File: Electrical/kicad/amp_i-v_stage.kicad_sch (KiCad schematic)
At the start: 26 parts, among them U1 NE5534ADR, U2 NE5534ADR, U3 NE5534ADR

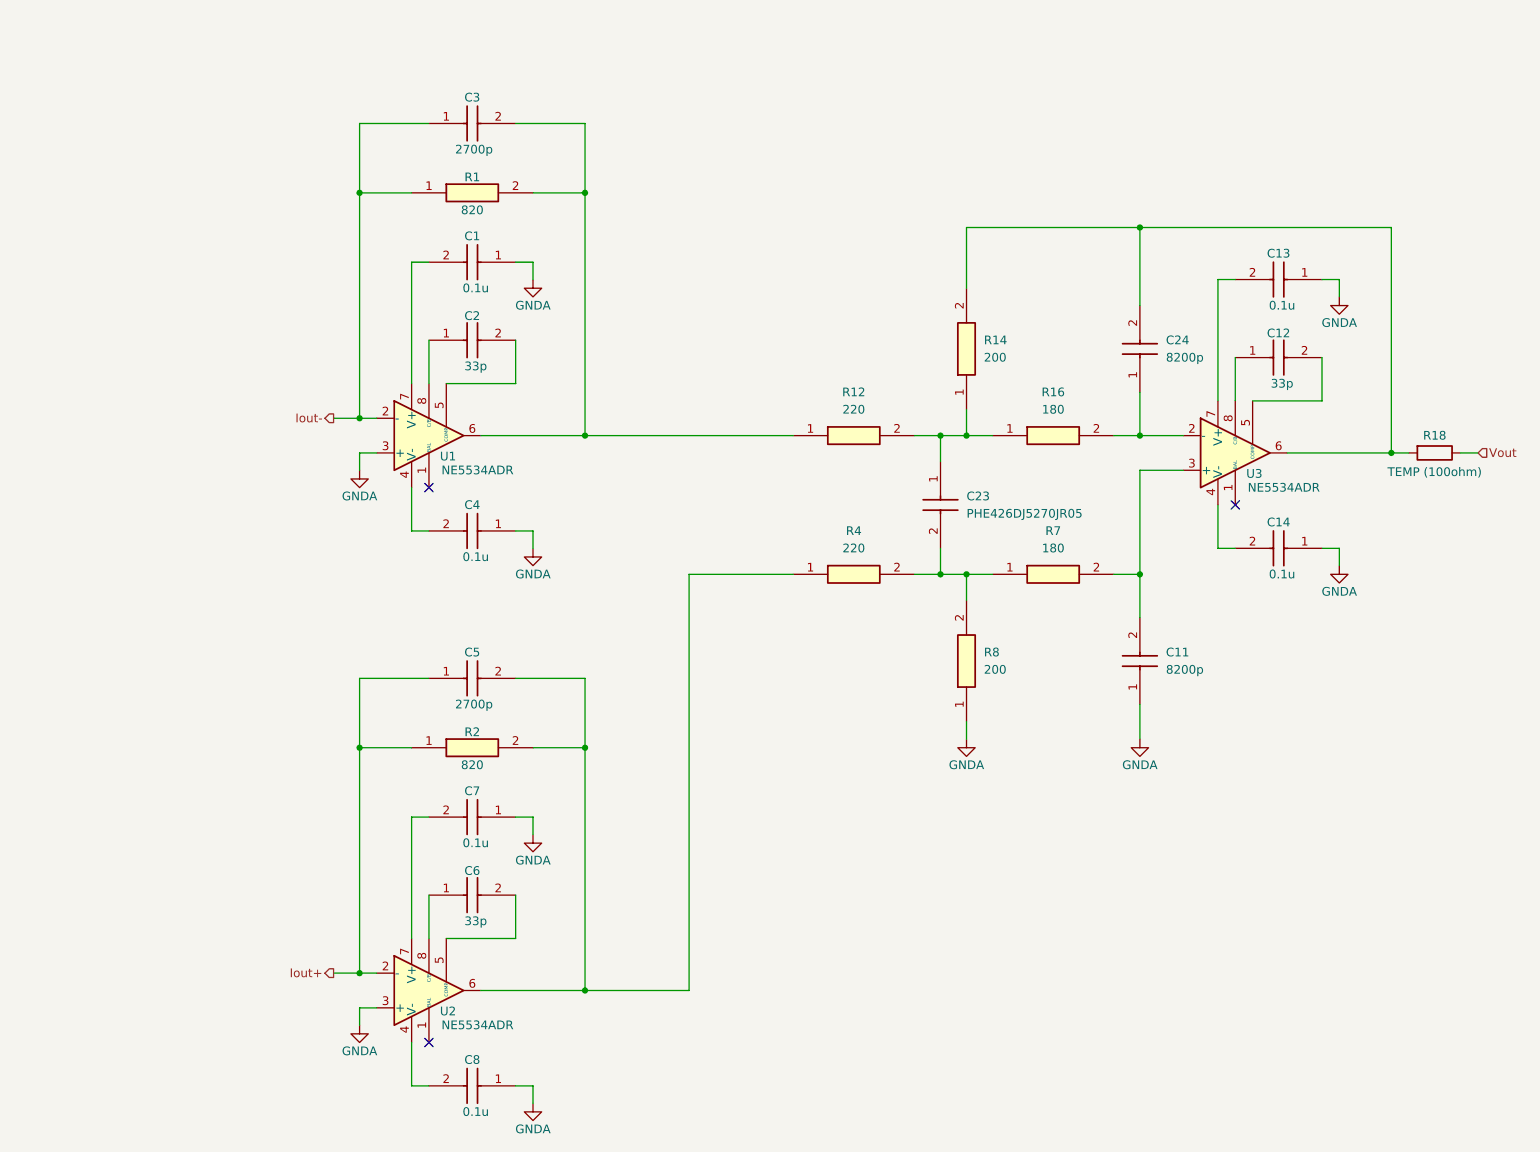
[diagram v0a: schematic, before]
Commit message: Updated PCM1795 schematic sheet
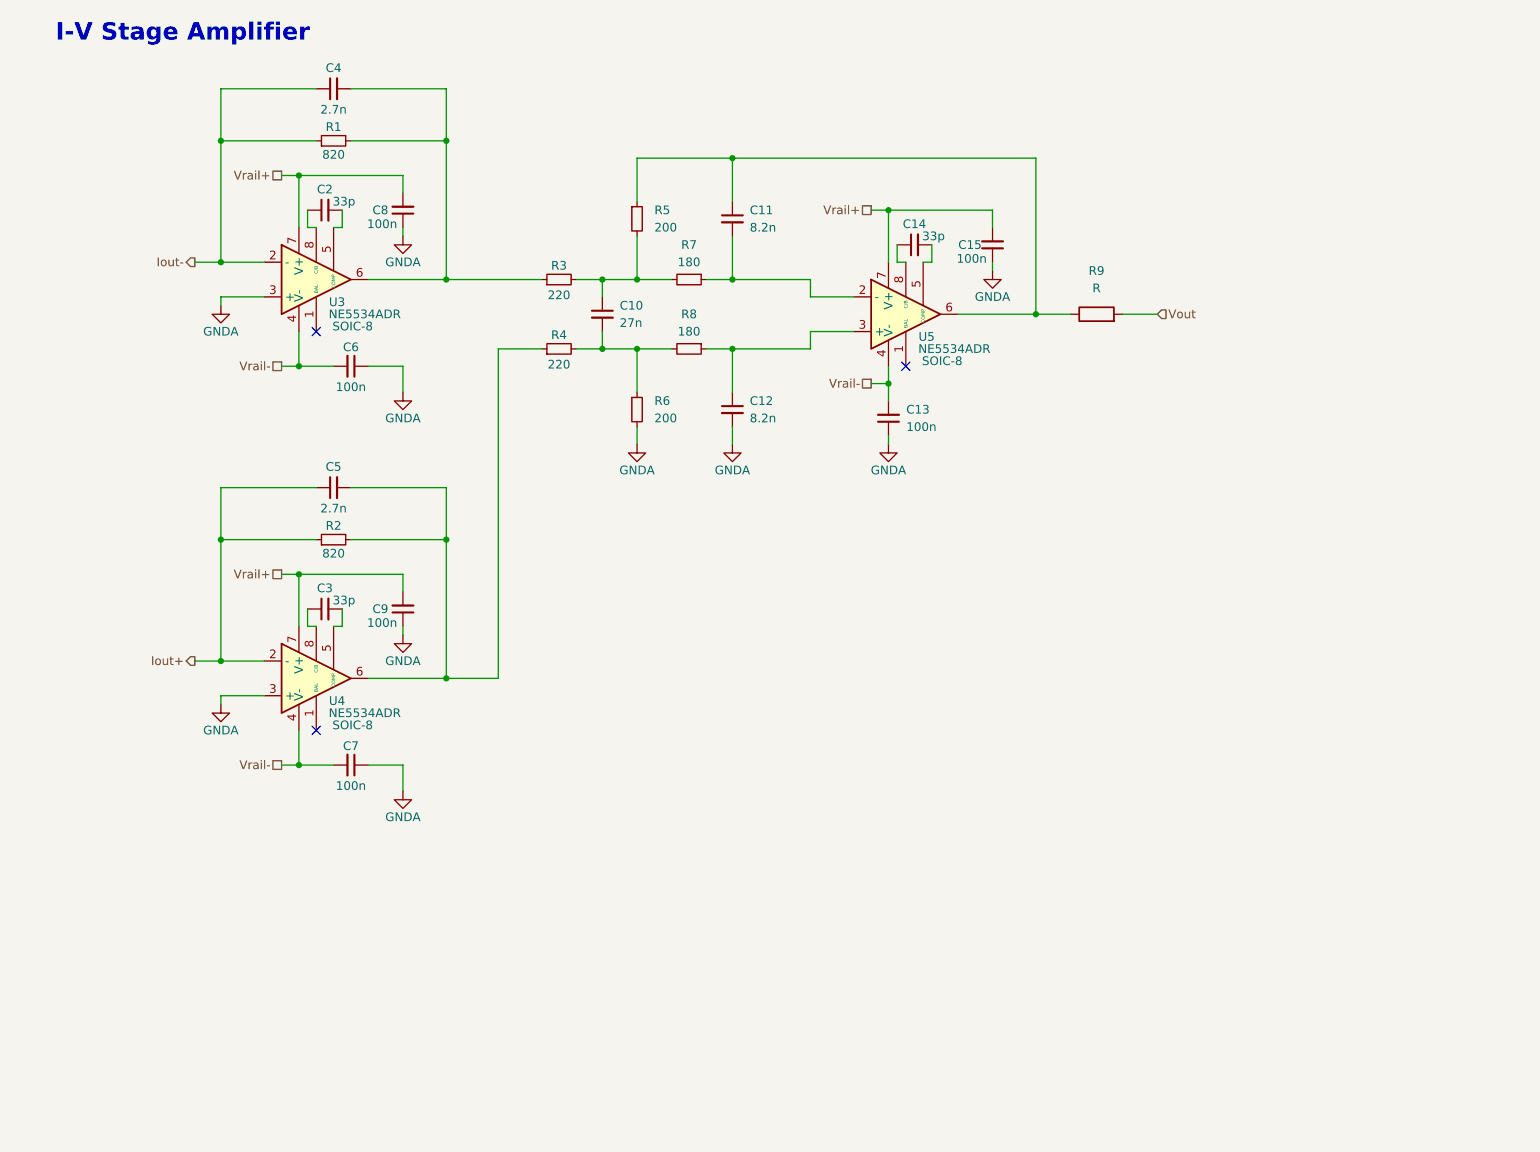
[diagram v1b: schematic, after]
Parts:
- removed C1, C13, C14, C4, C7, C8: 0.1u, PHE426HJ6100JR05, symbol Project_Library:PHE426HJ6100JR05
- removed C11, C24: 8200p, PHE426DJ4820JR05, symbol Project_Library:PHE426DJ4820JR05
- removed C12, C2, C6: 33p, FKP2O100331D00KSSD, symbol Project_Library:FKP2O100331D00KSSD
- removed C23: PHE426DJ5270JR05, PHE426DJ5270JR05, symbol Project_Library:PHE426DJ5270JR05
- removed C3, C5: 2700p, PHE426HJ4270JR05, symbol Project_Library:PHE426HJ4270JR05
- removed R1, R2: 820, ERA6AEB101V, symbol Project_Library:ERA-6AEB821V
- removed R12, R4: 220, ERA6AEB101V, symbol Project_Library:ERA-6AEB221V
- removed R14, R8: 200, ERA6AEB101V, symbol Project_Library:ERA-6AEB201V
- removed R16, R7: 180, ERA6AEB101V, symbol Project_Library:ERA-6AEB181V
- removed R18: TEMP (100ohm), symbol Device:R
- removed U1, U2, U3: NE5534ADR, Project_Library:SOIC127P600X175-8N, symbol Project_Library:NE5534ADR
- added C10: 27n, Project_Library:PHE426DJ5270JR05, symbol Project_Library:C_27n
- added C11, C12: 8.2n, Project_Library:PHE426DJ4820JR05, symbol Project_Library:C_8.2n
- added C13, C15, C6, C7, C8, C9: 100n, Project_Library:PHE426HJ6100JR05, symbol Project_Library:C_100n
- added C14, C2, C3: 33p, Project_Library:FKP2O100331D00KSSD, symbol Project_Library:C_33p
- added C4, C5: 2.7n, Project_Library:PHE426HJ4270JR05, symbol Project_Library:C_2.7n
- added R1, R2: 820, Project_Library:ERA6AEB101V, symbol Project_Library:R_820
- added R3, R4: 220, Project_Library:ERA6AEB101V, symbol Project_Library:R_220
- added R5, R6: 200, Project_Library:ERA6AEB101V, symbol Project_Library:R_200
- added R7, R8: 180, Project_Library:ERA6AEB101V, symbol Project_Library:R_180
- added R9: R, symbol Device:R
- added U3, U4, U5: NE5534ADR, Project_Library:SOIC127P600X175-8N, symbol Project_Library:U_NE5534ADR
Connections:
- net GNDA: now also C12.2, C13.1, C15.1, C6.1, C7.1, C8.1, C9.1, R6.2, U3.3 (+), U4.3 (+)
- net Iout+: now also C5.1, R2.1, U4.2 (-)
- net Iout-: now also C4.1, R1.1, U3.2 (-)
- net Vout: now also R9.2
- new net: C14.1, U5.8 (C/B)
- new net: C14.2, U5.5 (COMP)
- new net: C10.1, R3.2, R5.2, R7.2
- new net: C10.2, R4.2, R6.1, R8.2
- new net: C2.1, U3.8 (C/B)
- new net: C2.2, U3.5 (COMP)
- new net: C4.2, R1.2, R3.1, U3.6
- new net: C12.1, R8.1, U5.3 (+)
- new net: C5.2, R2.2, R4.1, U4.6
- new net: C11.2, R7.1, U5.2 (-)
- new net: C3.1, U4.8 (C/B)
- new net: C3.2, U4.5 (COMP)
- new net: C11.1, R5.1, R9.1, U5.6
- new net Vrail+: C15.2, C8.2, C9.2, U3.7 (V+), U4.7 (V+), U5.7 (V+)
- new net Vrail-: C13.2, C6.2, C7.2, U3.4 (V-), U4.4 (V-), U5.4 (V-)
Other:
- note added: "I-V Stage Amplifier"

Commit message: Added oscillator and crystal to schematic. Also did some refining of how things were laid out
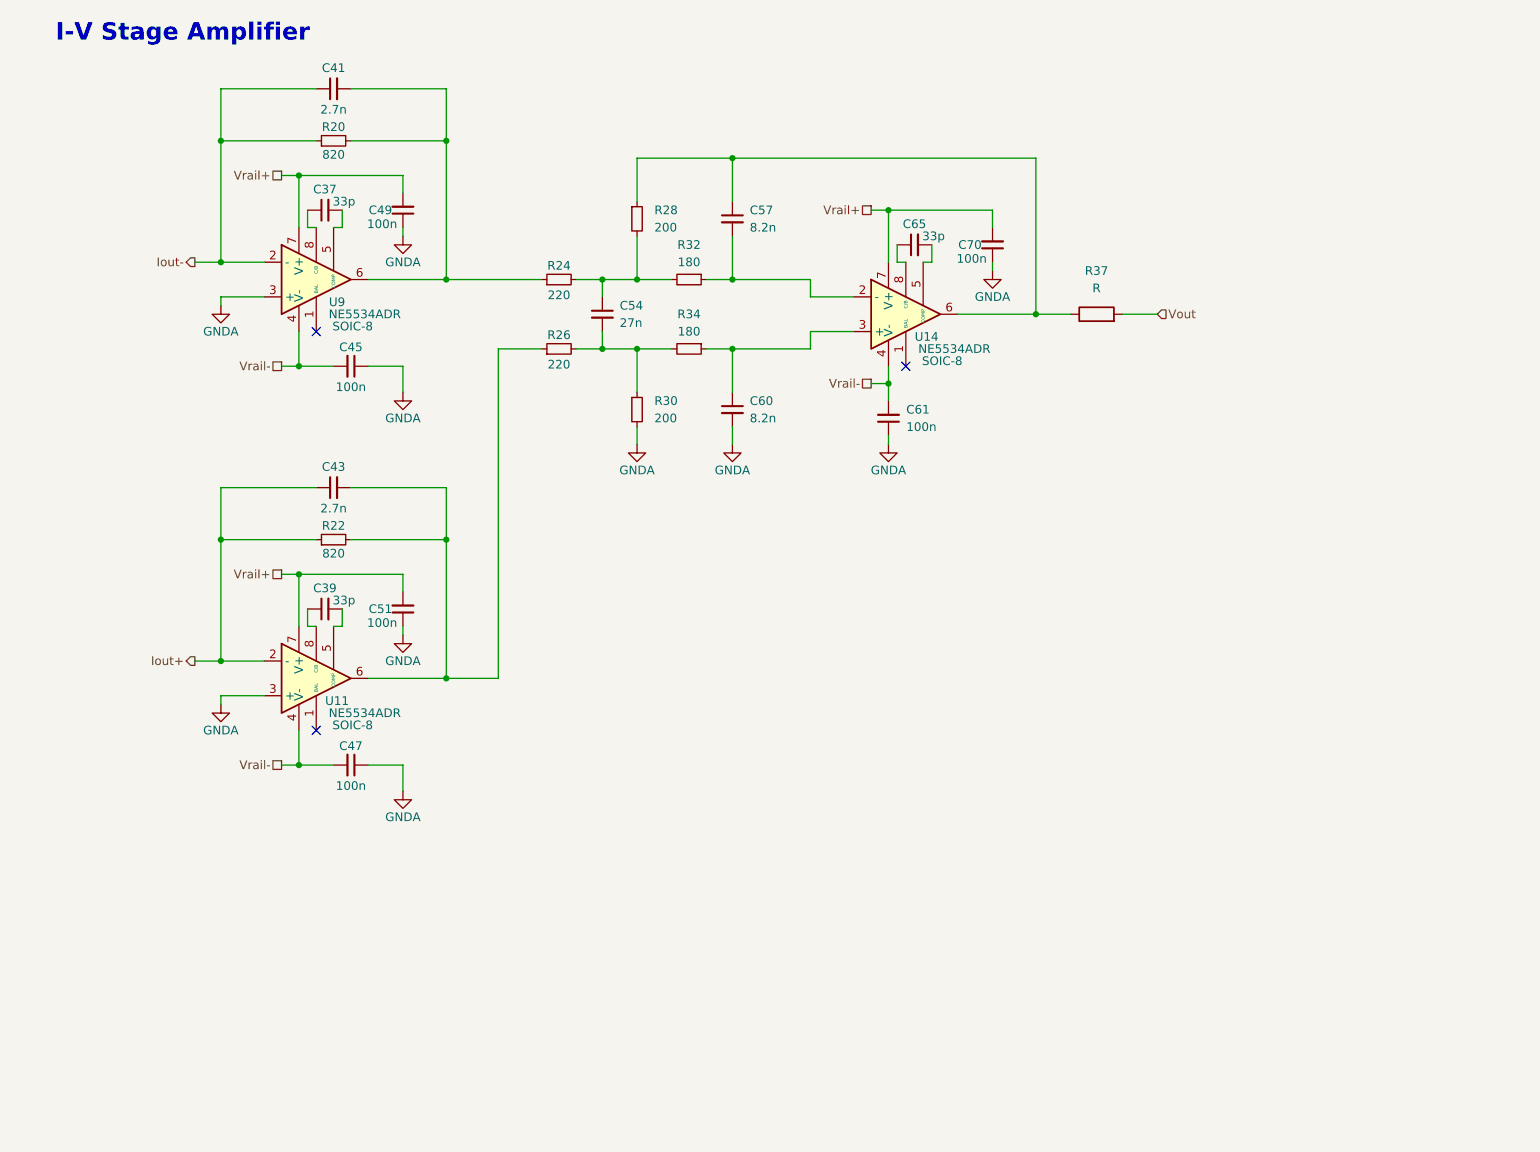
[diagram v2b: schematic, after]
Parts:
- renumbered C2 to C37, C3 to C39, C4 to C41, C5 to C43, C6 to C45, C7 to C47, C8 to C49, C9 to C51, C10 to C54, C11 to C57, C12 to C60, C13 to C61, C14 to C65, C15 to C70, R1 to R20, R2 to R22, R3 to R24, R4 to R26, R5 to R28, R6 to R30, R7 to R32, R8 to R34, R9 to R37, U4 to U11, U5 to U14, U3 to U9
